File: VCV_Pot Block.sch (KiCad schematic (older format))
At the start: 21 parts, among them U3 CD74HC4067M

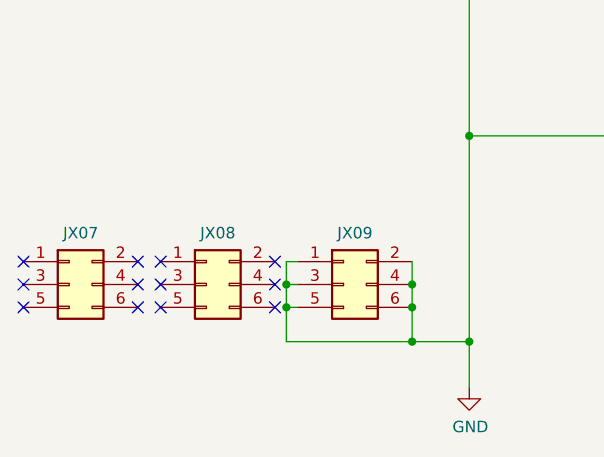
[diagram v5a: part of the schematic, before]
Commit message: Rails done, GND corrected.
Now for checking and decals
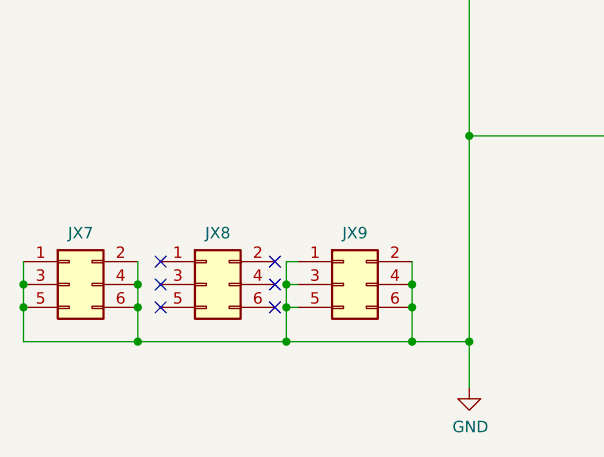
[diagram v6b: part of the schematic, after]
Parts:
- renumbered JX07 to JX7, JX08 to JX8, JX09 to JX9
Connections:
- net GND: now also JX7.1 (Pin_1), JX7.2 (Pin_2), JX7.3 (Pin_3), JX7.4 (Pin_4), JX7.5 (Pin_5), JX7.6 (Pin_6)
- no-connect marks 12 -> 6
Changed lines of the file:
@@
 $Descr A4 11693 8268
 encoding utf-8
-Sheet 4 8
+Sheet 4 9
 Title "cp_midi_controller_002"
 Date "2019-01-13"
@@
 P 950 7000
 AR Path="/5C4B73B3/5D8F0D68" Ref="JX?"  Part="1"
-AR Path="/5C3B66BD/5D8F0D68" Ref="JX07"  Part="1"
-F 0 "JX07" H 1000 7225 50  0000 C CNN
+AR Path="/5C3B66BD/5D8F0D68" Ref="JX7"  Part="1"
+F 0 "JX7" H 1000 7225 50  0000 C CNN
 F 1 "Conn_02x03_Odd_Even" H 1000 7226 50  0001 C CNN
 F 2 "Connector_PinHeader_2.54mm:PinHeader_2x03_P2.54mm_Vertical" H 950 7000 50  0001 C CNN
@@
 P 2150 7000
 AR Path="/5C4B73B3/5D8F0D6F" Ref="JX?"  Part="1"
-AR Path="/5C3B66BD/5D8F0D6F" Ref="JX09"  Part="1"
-F 0 "JX09" H 2200 7225 50  0000 C CNN
+AR Path="/5C3B66BD/5D8F0D6F" Ref="JX9"  Part="1"
+F 0 "JX9" H 2200 7225 50  0000 C CNN
 F 1 "Conn_02x03_Odd_Even" H 2200 7226 50  0001 C CNN
 F 2 "Connector_PinHeader_2.54mm:PinHeader_2x03_P2.54mm_Vertical" H 2150 7000 50  0001 C CNN
@@
 P 1550 7000
 AR Path="/5C4B73B3/5D8F0D7F" Ref="JX?"  Part="1"
-AR Path="/5C3B66BD/5D8F0D7F" Ref="JX08"  Part="1"
-F 0 "JX08" H 1600 7225 50  0000 C CNN
+AR Path="/5C3B66BD/5D8F0D7F" Ref="JX8"  Part="1"
+F 0 "JX8" H 1600 7225 50  0000 C CNN
 F 1 "Conn_02x03_Odd_Even" H 1600 7226 50  0001 C CNN
 F 2 "Connector_PinHeader_2.54mm:PinHeader_2x03_P2.54mm_Vertical" H 1550 7000 50  0001 C CNN
@@
 NoConn ~ 1350 7000
 NoConn ~ 1350 6900
-NoConn ~ 1250 6900
-NoConn ~ 1250 7000
-NoConn ~ 1250 7100
-NoConn ~ 750  6900
-NoConn ~ 750  7000
-NoConn ~ 750  7100
 Wire Wire Line
 	2700 6350 2700 7250
@@
 Wire Wire Line
 	1750 2450 2200 2450
+Wire Wire Line
+	1250 6900 1250 7000
+Wire Wire Line
+	1250 7250 1900 7250
+Connection ~ 1250 7000
+Wire Wire Line
+	1250 7000 1250 7100
+Connection ~ 1250 7100
+Wire Wire Line
+	1250 7100 1250 7250
+Connection ~ 1900 7250
+Wire Wire Line
+	750  6900 750  7000
+Wire Wire Line
+	750  7250 1250 7250
+Connection ~ 750  7000
+Wire Wire Line
+	750  7000 750  7100
+Connection ~ 750  7100
+Wire Wire Line
+	750  7100 750  7250
+Connection ~ 1250 7250
 $EndSCHEMATC
